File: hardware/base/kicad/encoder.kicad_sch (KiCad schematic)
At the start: 42 parts, among them J6 HC-WK88-H132-1X2-55B, SW2 TERM A B Z, U21 TPS1H000AQDGNRQ1, U22 AM26LV32EIDR

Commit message: Lanes no longer shadowed in the assembly; channel assignments carried; encoder sheet drawn from the wired channels; trunk drop found across the board
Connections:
- net B: now also U22.13 (4Y); no longer U22.5 (2Y)
- net Z: now also U22.5 (2Y); no longer U22.11 (3Y)
- net at D31.3 (COM), R91.2, R92.1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: now also U22.14 (4A); no longer U22.6 (2A)
- net at D32.3 (COM), R94.2, R95.1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: now also U22.15 (4B); no longer U22.7 (2B)
- net at D34.3 (COM), R102.2, R103.1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: now also U22.7 (2B); no longer U22.9 (3B)
- net at D33.3 (COM), R100.1, R101.1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: now also U22.6 (2A); no longer U22.10 (3A)

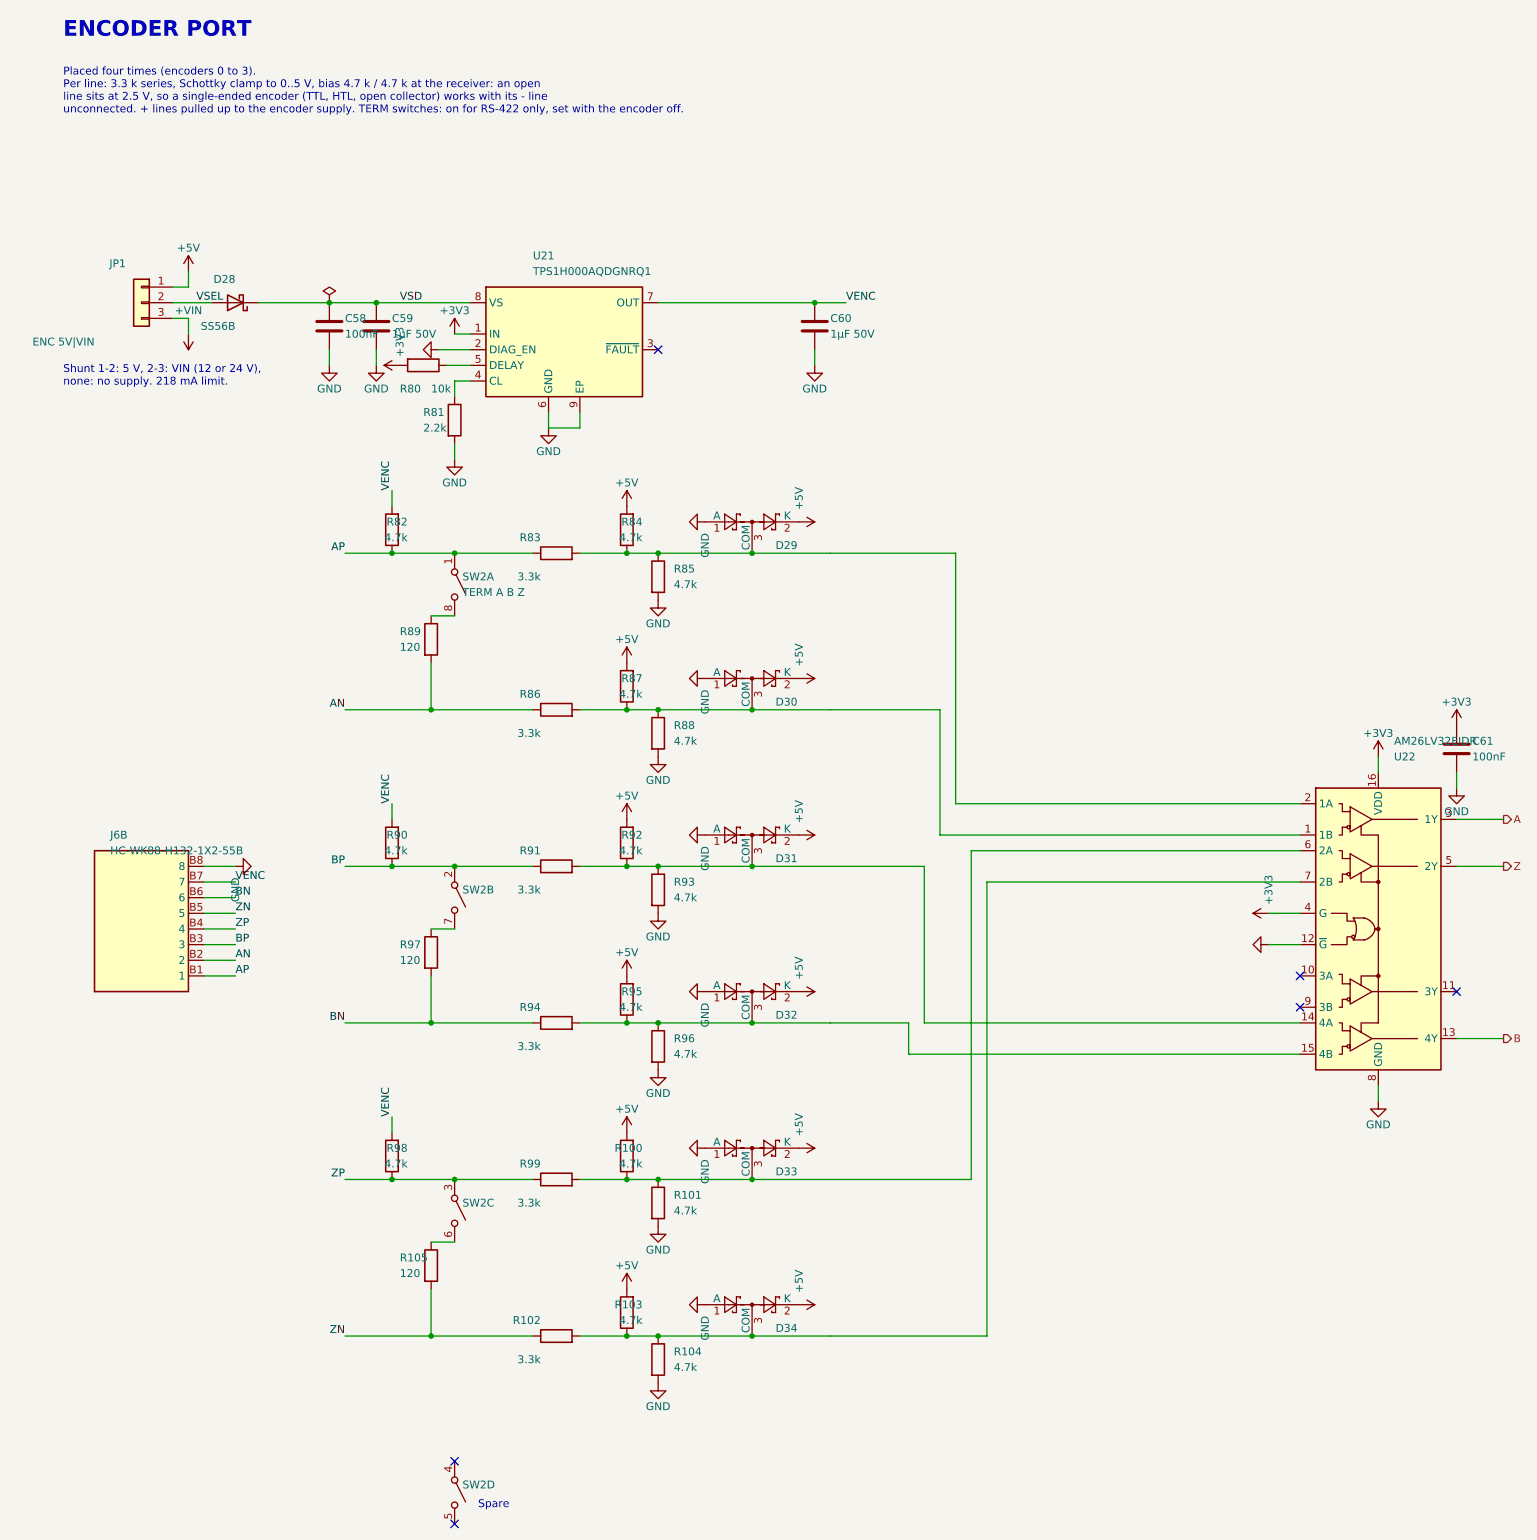
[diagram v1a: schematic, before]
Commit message: Encoder inputs: no termination switch on the board; an RS-422 encoder on a long or fast line takes its 120 ohm at the end of its cable
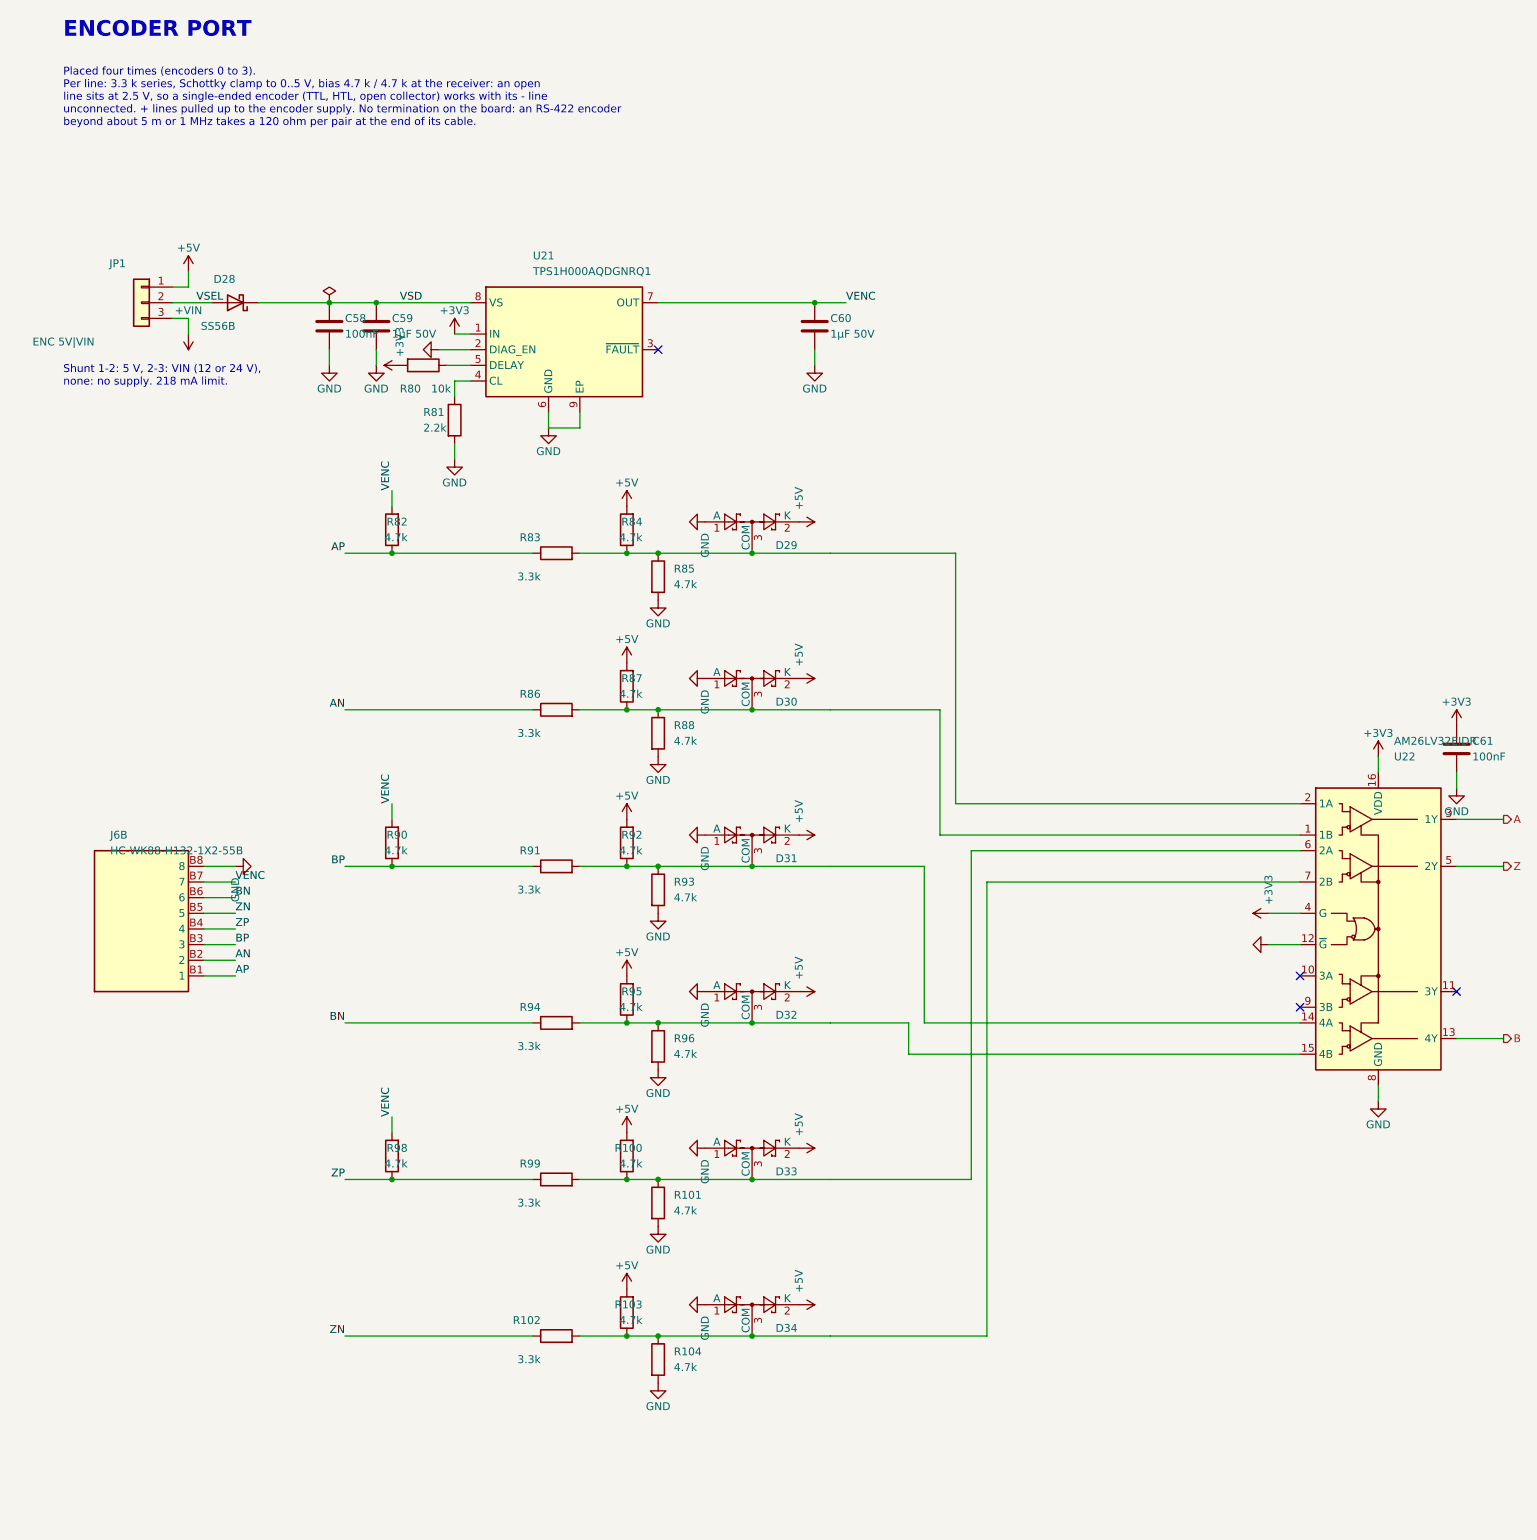
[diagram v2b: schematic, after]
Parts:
- removed R105, R89, R97: 120, Resistor_SMD:R_0603_1608Metric, symbol Device:R
- removed SW2: TERM A B Z, Button_Switch_SMD:SW_DIP_SPSTx04_Slide_KingTek_DSHP04TS_W7.62mm_P1.27mm, symbol Bornier:SW_DIP_x04_Split
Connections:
- no-connect marks 6 -> 4
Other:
- note added: "Placed four times (encoders 0 to 3). Per line: 3.3 k series, Schottky clamp to 0..5 V, bias 4.7 k / 4.7 k at the receiver: an open line sits at 2.5 V, so a single-ended encoder (TTL, HTL, open collector) works with its - line unconnected. + lines pulled up to the encoder supply. No termination on the board: an RS-422 encoder beyond about 5 m or 1 MHz takes a 120 ohm per pair at the end of its cab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"
- note removed: "Placed four times (encoders 0 to 3). Per line: 3.3 k series, Schottky clamp to 0..5 V, bias 4.7 k / 4.7 k at the receiver: an open line sits at 2.5 V, so a single-ended encoder (TTL, HTL, open collector) works with its - line unconnected. + lines pulled up to the encoder supply. TERM switches: on for RS-422 only, set with the encoder off."
- note removed: "Spare"
